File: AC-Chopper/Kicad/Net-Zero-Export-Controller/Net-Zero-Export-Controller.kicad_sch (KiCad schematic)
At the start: 0 parts

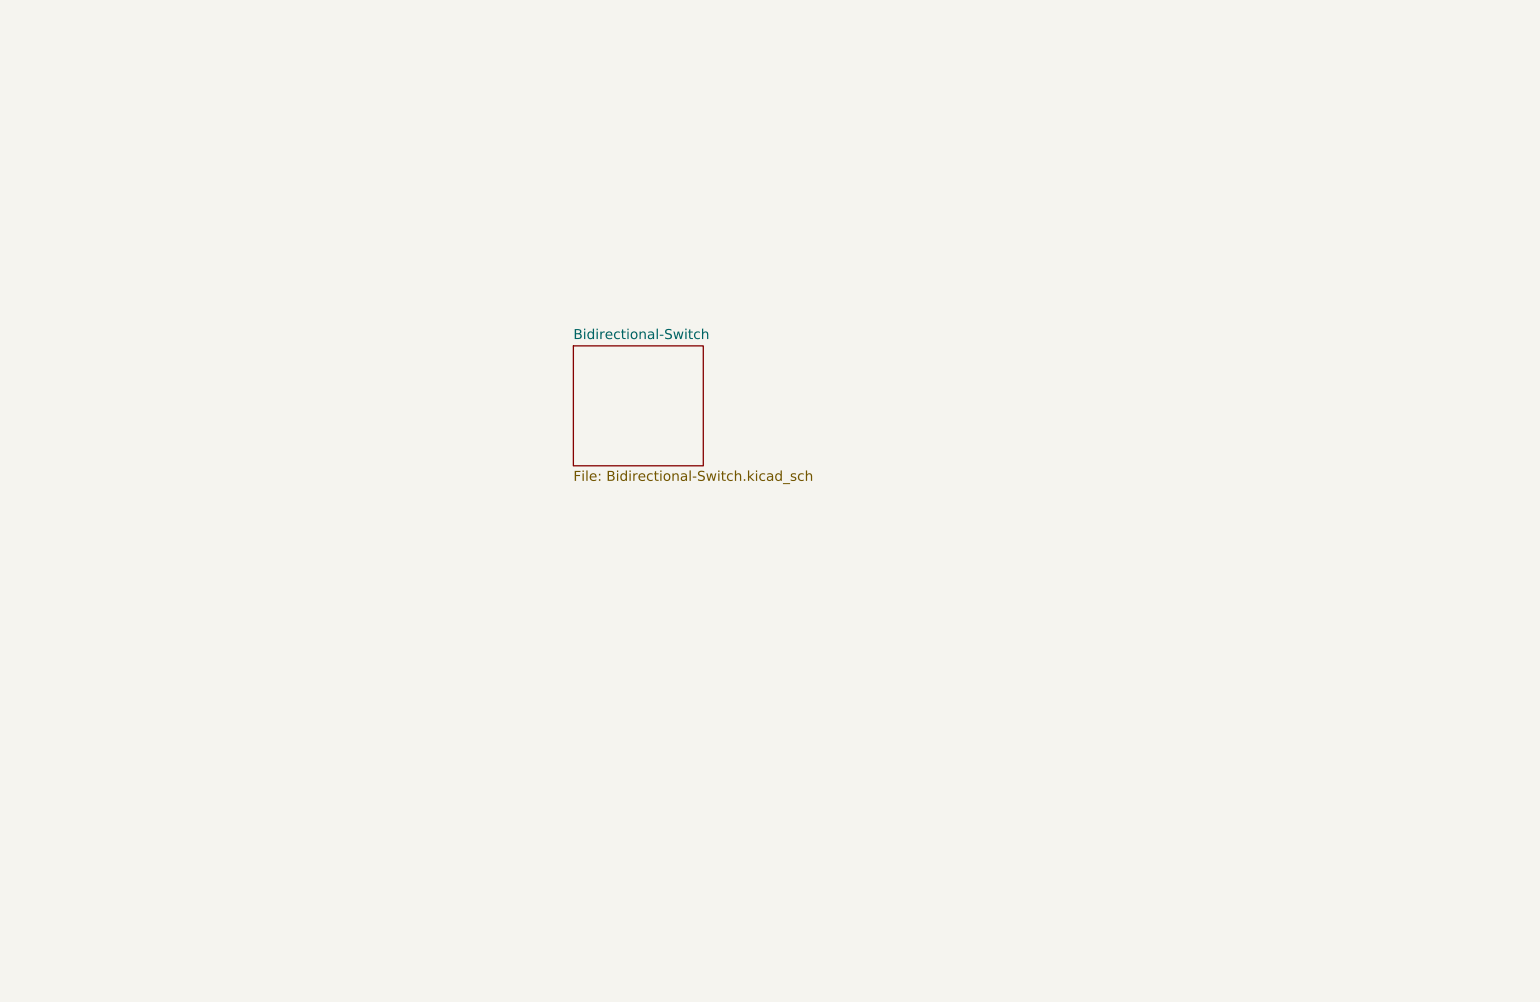
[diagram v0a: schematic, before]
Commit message: Added new work done ac chopper power controll testing, new AC AC buck and pcb
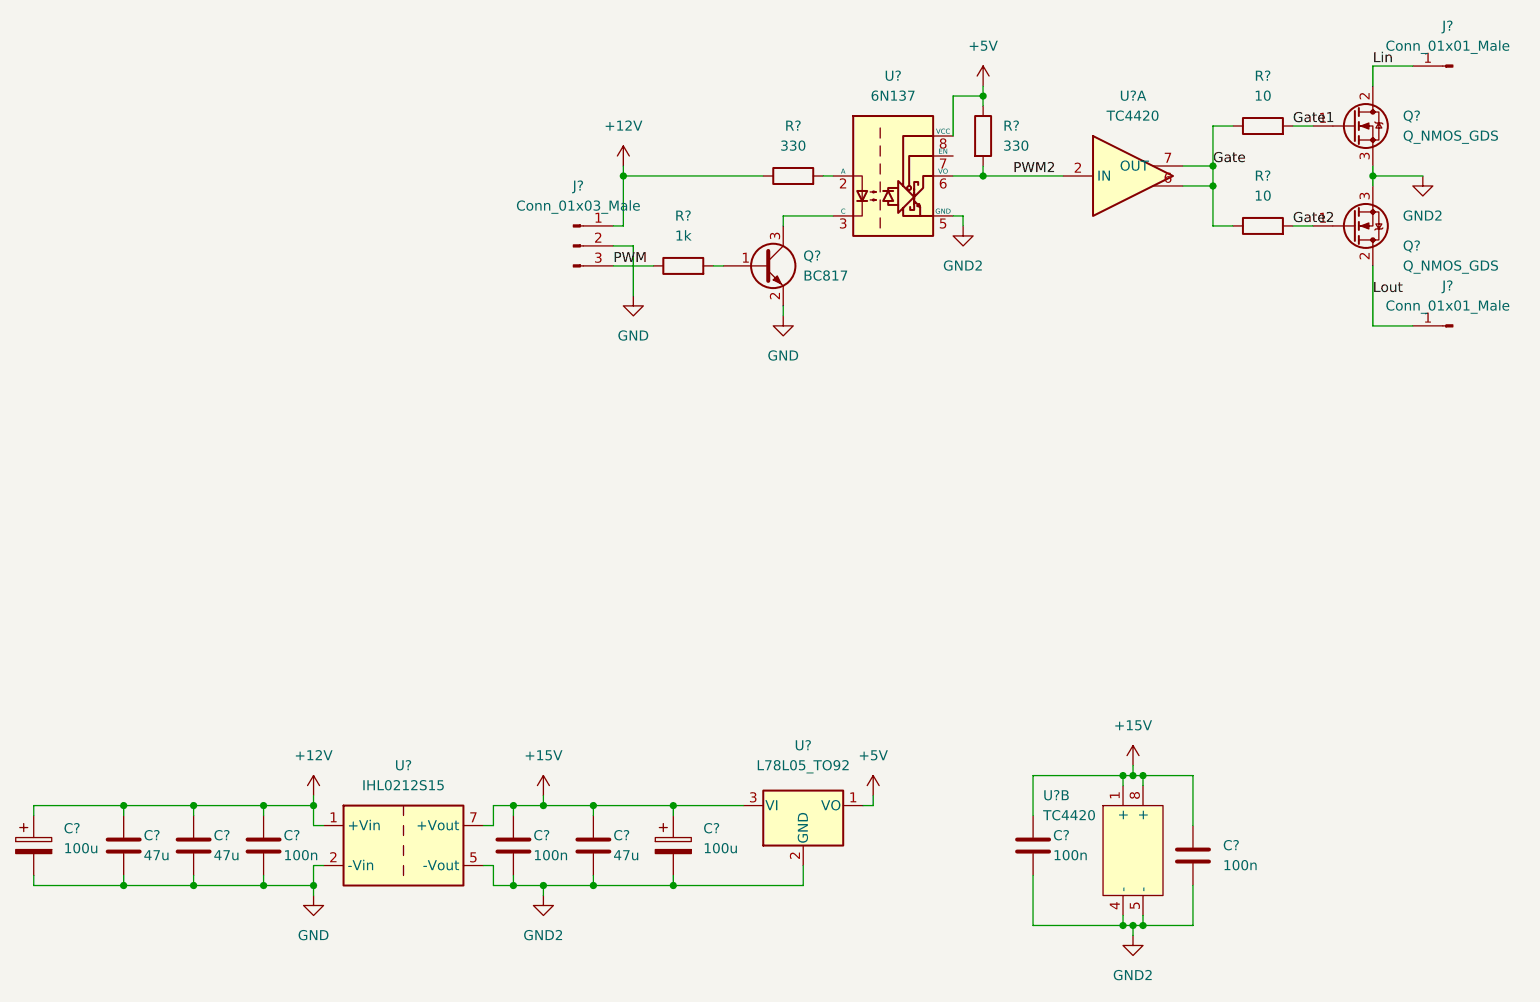
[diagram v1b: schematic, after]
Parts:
- added C? (x3): 47u, Capacitor_SMD:C_1206_3216Metric_Pad1.33x1.80mm_HandSolder, symbol Device:C
- added C? (x2): 100n, Capacitor_SMD:C_0603_1608Metric_Pad1.08x0.95mm_HandSolder, symbol Device:C
- added C? (x2): 100n, symbol Device:C
- added C? (x2): 100u, Capacitor_THT:CP_Radial_D10.0mm_P5.00mm, symbol Device:C_Polarized
- added J? (x2): Conn_01x01_Male, TerminalBlock:Spade-Terminal, symbol Connector:Conn_01x01_Male
- added J?: Conn_01x03_Male, Connector_PinHeader_2.54mm:PinHeader_1x03_P2.54mm_Vertical, symbol Connector:Conn_01x03_Male
- added Q? (x2): Q_NMOS_GDS, Package_TO_SOT_THT:TO-220F-3_Vertical, symbol Device:Q_NMOS_GDS
- added Q?: BC817, Package_TO_SOT_SMD:SOT-23, symbol Transistor_BJT:BC817
- added R?: 1k, Resistor_SMD:R_1206_3216Metric_Pad1.30x1.75mm_HandSolder, symbol Device:R
- added R? (x2): 10, Resistor_SMD:R_1206_3216Metric_Pad1.30x1.75mm_HandSolder, symbol Device:R
- added R?: 330, Resistor_THT:R_Axial_DIN0207_L6.3mm_D2.5mm_P7.62mm_Horizontal, symbol Device:R
- added R?: 330, Resistor_SMD:R_1206_3216Metric_Pad1.30x1.75mm_HandSolder, symbol Device:R
- added U?: 6N137, Package_DIP:DIP-8_W7.62mm_LongPads, symbol Isolator:6N137
- added U? (x2): TC4420, Package_DIP:DIP-8_W7.62mm_LongPads, symbol Driver_FET:TC4420
- added U?: L78L05_TO92, Package_TO_SOT_THT:TO-92_Inline_Wide, symbol Regulator_Linear:L78L05_TO92
- added U?: IHL0212S15, Converter_DCDC:IHL-Series, symbol Converter_DCDC:IHL0212S15
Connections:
- new net: Q?.1 (B), R?.2
- new net: R?.2, U?.2 (A)
- new net: Q?.3 (C), U?.3 (C)
- new net +12V: C?.1, C?.1, C?.1, C?.1, J?.1 (Pin_1), R?.1, U?.1 (+Vin)
- new net +15V: C?.1, C?.1, C?.1, C?.1, C?.1, U?.1 (+), U?.3 (VI), U?.7 (+Vout), U?.8 (+)
- new net +5V: R?.1, U?.1 (VO), U?.8 (VCC)
- new net GND: C?.2, C?.2, C?.2, C?.2, J?.2 (Pin_2), Q?.2 (E), U?.2 (-Vin)
- new net GND2: C?.2, C?.2, C?.2, C?.2, C?.2, Q?.3 (S), Q?.3 (S), U?.2 (GND), U?.4 (-), U?.5 (-), U?.5 (-Vout), U?.5 (GND)
- new net Gate: R?.1, R?.1, U?.6, U?.7 (OUT)
- new net Gate1: Q?.1 (G), R?.2
- new net Gate2: Q?.1 (G), R?.2
- new net Lin: J?.1 (Pin_1), Q?.2 (D)
- new net Lout: J?.1 (Pin_1), Q?.2 (D)
- new net PWM: J?.3 (Pin_3), R?.1
- new net PWM2: R?.2, U?.2 (IN), U?.6 (VO)
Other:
- removed sheet Bidirectional-Switch
